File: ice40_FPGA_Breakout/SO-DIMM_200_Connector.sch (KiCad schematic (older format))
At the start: 21 parts

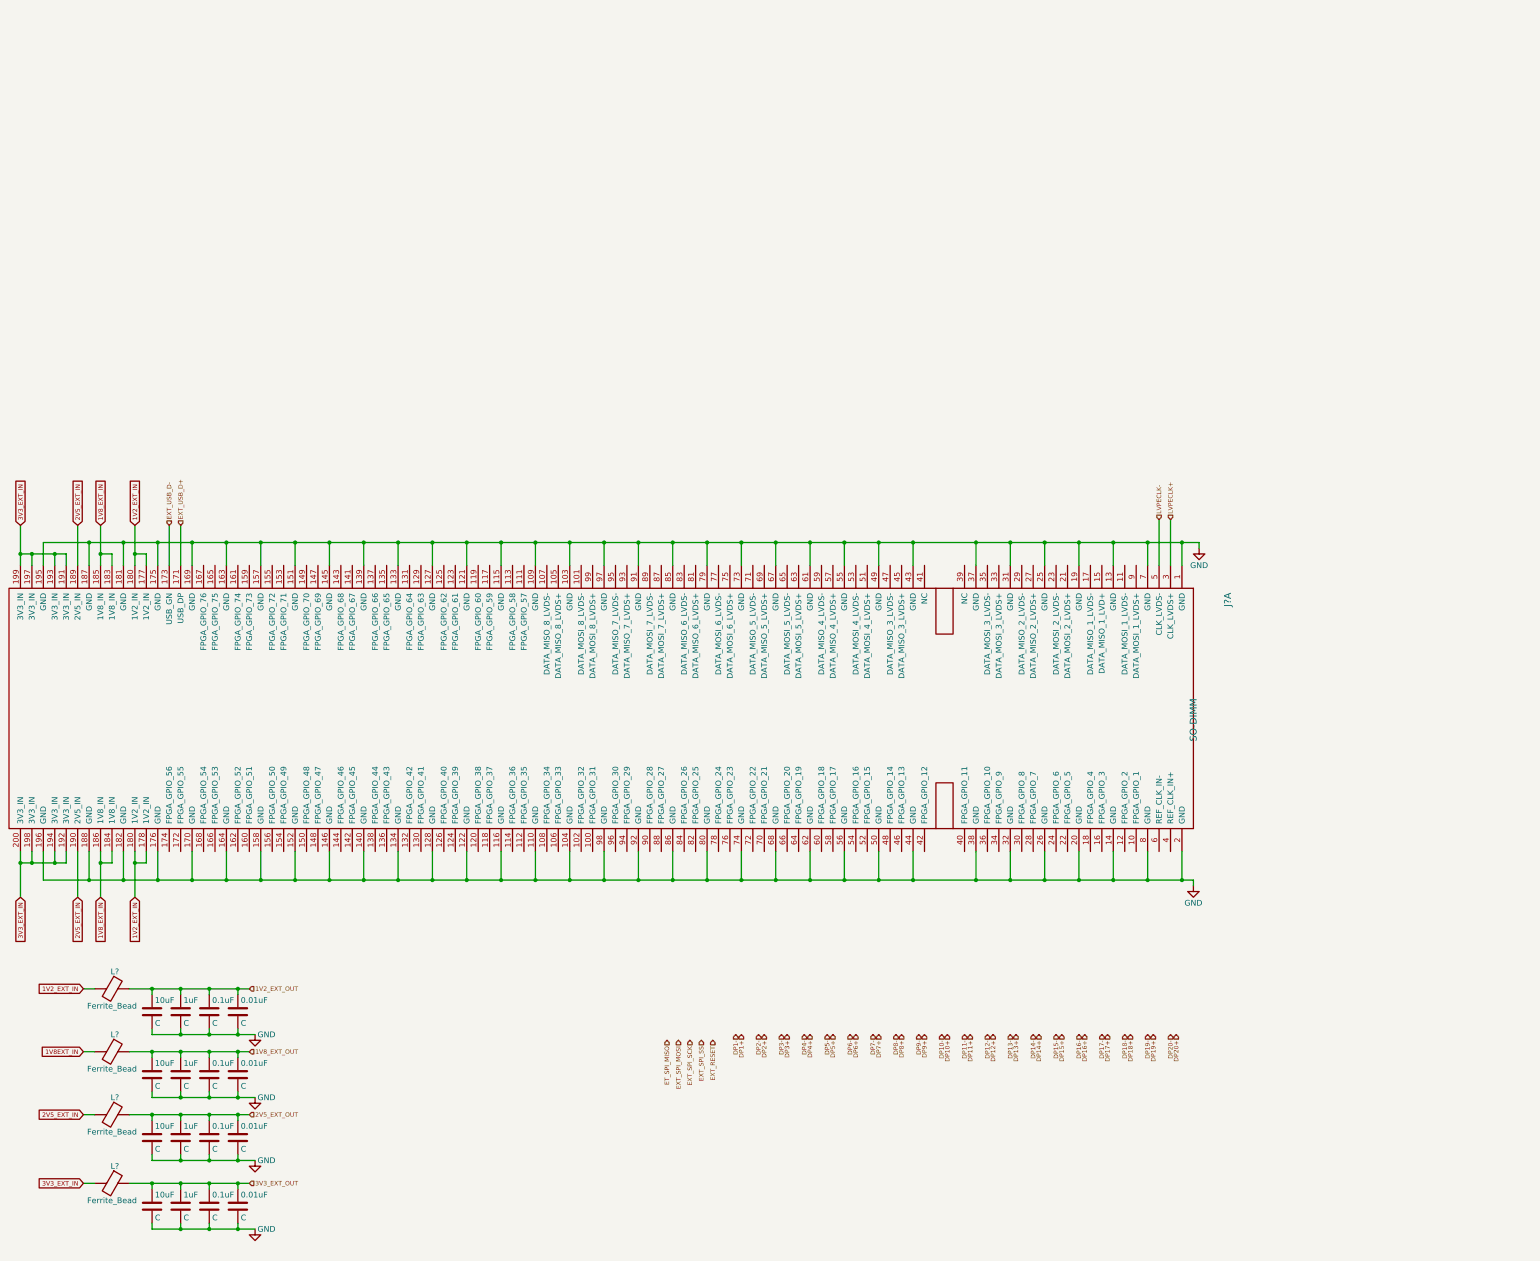
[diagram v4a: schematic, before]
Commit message: Component Annotated and R/C/Conn/TP CVPCB mapping
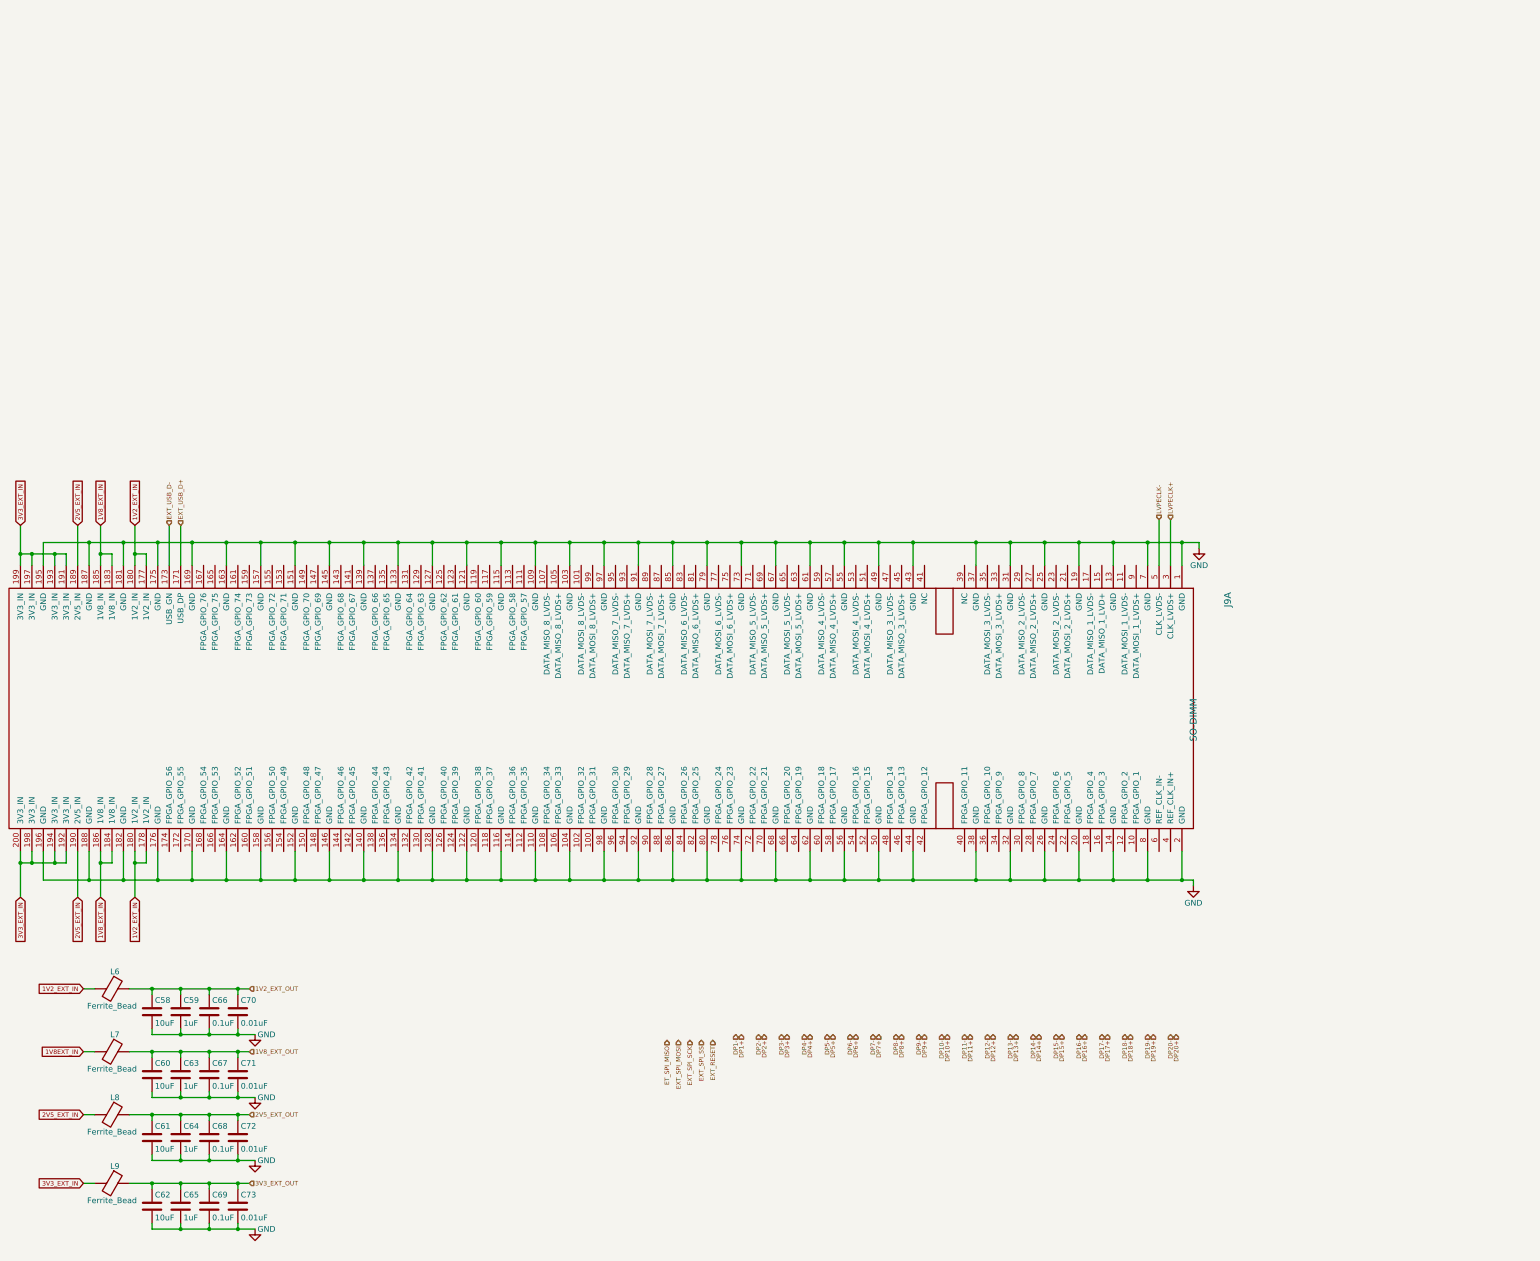
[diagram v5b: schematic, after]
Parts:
- C58, C60, C61, C62: renamed from 10uF; value C -> 10uF
- C59, C63, C64, C65: renamed from 1uF; value C -> 1uF
- C66, C67, C68, C69: renamed from 0.1uF; value C -> 0.1uF
- C70, C71, C72, C73: renamed from 0.01uF; value C -> 0.01uF
- gave numbers to parts that had none: 5
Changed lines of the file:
@@
 $EndDescr
 $Comp
-L SO-DIMM J?
+L SO-DIMM J9
 U 1 1 5A3A8985
 P 11200 2950
-F 0 "J?" H 10250 3100 60  0000 C CNN
+F 0 "J9" H 10250 3100 60  0000 C CNN
 F 1 "SO-DIMM" H 11300 2800 60  0000 C CNN
 F 2 "" H 11350 2950 60  0001 C CNN
@@
 $EndComp
 $Comp
-L C 10uF
+L C C58
 U 1 1 5A418459
 P 1950 5600
-F 0 "10uF" H 1975 5700 50  0000 L CNN
-F 1 "C" H 1975 5500 50  0000 L CNN
+F 0 "C58" H 1975 5700 50  0000 L CNN
+F 1 "10uF" H 1975 5500 50  0000 L CNN
 F 2 "" H 1988 5450 50  0001 C CNN
 F 3 "" H 1950 5600 50  0001 C CNN
@@
 $EndComp
 $Comp
-L C 1uF
+L C C59
 U 1 1 5A4184EA
 P 2200 5600
-F 0 "1uF" H 2225 5700 50  0000 L CNN
-F 1 "C" H 2225 5500 50  0000 L CNN
+F 0 "C59" H 2225 5700 50  0000 L CNN
+F 1 "1uF" H 2225 5500 50  0000 L CNN
 F 2 "" H 2238 5450 50  0001 C CNN
 F 3 "" H 2200 5600 50  0001 C CNN
@@
 $EndComp
 $Comp
-L C 0.1uF
+L C C66
 U 1 1 5A41850F
 P 2450 5600
-F 0 "0.1uF" H 2475 5700 50  0000 L CNN
-F 1 "C" H 2475 5500 50  0000 L CNN
+F 0 "C66" H 2475 5700 50  0000 L CNN
+F 1 "0.1uF" H 2475 5500 50  0000 L CNN
 F 2 "" H 2488 5450 50  0001 C CNN
 F 3 "" H 2450 5600 50  0001 C CNN
@@
 $EndComp
 $Comp
-L C 0.01uF
+L C C70
 U 1 1 5A418541
 P 2700 5600
-F 0 "0.01uF" H 2725 5700 50  0000 L CNN
-F 1 "C" H 2725 5500 50  0000 L CNN
+F 0 "C70" H 2725 5700 50  0000 L CNN
+F 1 "0.01uF" H 2725 5500 50  0000 L CNN
 F 2 "" H 2738 5450 50  0001 C CNN
 F 3 "" H 2700 5600 50  0001 C CNN
@@
 $EndComp
 $Comp
-L C 10uF
+L C C60
 U 1 1 5A41856A
 P 1950 6150
-F 0 "10uF" H 1975 6250 50  0000 L CNN
-F 1 "C" H 1975 6050 50  0000 L CNN
+F 0 "C60" H 1975 6250 50  0000 L CNN
+F 1 "10uF" H 1975 6050 50  0000 L CNN
 F 2 "" H 1988 6000 50  0001 C CNN
 F 3 "" H 1950 6150 50  0001 C CNN
@@
 $EndComp
 $Comp
-L C 1uF
+L C C63
 U 1 1 5A4185BC
 P 2200 6150
-F 0 "1uF" H 2225 6250 50  0000 L CNN
-F 1 "C" H 2225 6050 50  0000 L CNN
+F 0 "C63" H 2225 6250 50  0000 L CNN
+F 1 "1uF" H 2225 6050 50  0000 L CNN
 F 2 "" H 2238 6000 50  0001 C CNN
 F 3 "" H 2200 6150 50  0001 C CNN
@@
 $EndComp
 $Comp
-L C 0.1uF
+L C C67
 U 1 1 5A4185F9
 P 2450 6150
-F 0 "0.1uF" H 2475 6250 50  0000 L CNN
-F 1 "C" H 2475 6050 50  0000 L CNN
+F 0 "C67" H 2475 6250 50  0000 L CNN
+F 1 "0.1uF" H 2475 6050 50  0000 L CNN
 F 2 "" H 2488 6000 50  0001 C CNN
 F 3 "" H 2450 6150 50  0001 C CNN
@@
 $EndComp
 $Comp
-L C 0.01uF
+L C C71
 U 1 1 5A41862F
 P 2700 6150
-F 0 "0.01uF" H 2725 6250 50  0000 L CNN
-F 1 "C" H 2725 6050 50  0000 L CNN
+F 0 "C71" H 2725 6250 50  0000 L CNN
+F 1 "0.01uF" H 2725 6050 50  0000 L CNN
 F 2 "" H 2738 6000 50  0001 C CNN
 F 3 "" H 2700 6150 50  0001 C CNN
@@
 $EndComp
 $Comp
-L C 10uF
+L C C61
 U 1 1 5A418664
 P 1950 6700
-F 0 "10uF" H 1975 6800 50  0000 L CNN
-F 1 "C" H 1975 6600 50  0000 L CNN
+F 0 "C61" H 1975 6800 50  0000 L CNN
+F 1 "10uF" H 1975 6600 50  0000 L CNN
 F 2 "" H 1988 6550 50  0001 C CNN
 F 3 "" H 1950 6700 50  0001 C CNN
@@
 $EndComp
 $Comp
-L C 1uF
+L C C64
 U 1 1 5A4186B2
 P 2200 6700
-F 0 "1uF" H 2225 6800 50  0000 L CNN
-F 1 "C" H 2225 6600 50  0000 L CNN
+F 0 "C64" H 2225 6800 50  0000 L CNN
+F 1 "1uF" H 2225 6600 50  0000 L CNN
 F 2 "" H 2238 6550 50  0001 C CNN
 F 3 "" H 2200 6700 50  0001 C CNN
@@
 $EndComp
 $Comp
-L C 0.1uF
+L C C68
 U 1 1 5A4186E9
 P 2450 6700
-F 0 "0.1uF" H 2475 6800 50  0000 L CNN
-F 1 "C" H 2475 6600 50  0000 L CNN
+F 0 "C68" H 2475 6800 50  0000 L CNN
+F 1 "0.1uF" H 2475 6600 50  0000 L CNN
 F 2 "" H 2488 6550 50  0001 C CNN
 F 3 "" H 2450 6700 50  0001 C CNN
@@
 $EndComp
 $Comp
-L C 0.01uF
+L C C72
 U 1 1 5A418729
 P 2700 6700
-F 0 "0.01uF" H 2725 6800 50  0000 L CNN
-F 1 "C" H 2725 6600 50  0000 L CNN
+F 0 "C72" H 2725 6800 50  0000 L CNN
+F 1 "0.01uF" H 2725 6600 50  0000 L CNN
 F 2 "" H 2738 6550 50  0001 C CNN
 F 3 "" H 2700 6700 50  0001 C CNN
@@
 $EndComp
 $Comp
-L C 10uF
+L C C62
 U 1 1 5A418776
 P 1950 7300
-F 0 "10uF" H 1975 7400 50  0000 L CNN
-F 1 "C" H 1975 7200 50  0000 L CNN
+F 0 "C62" H 1975 7400 50  0000 L CNN
+F 1 "10uF" H 1975 7200 50  0000 L CNN
 F 2 "" H 1988 7150 50  0001 C CNN
 F 3 "" H 1950 7300 50  0001 C CNN
@@
 $EndComp
 $Comp
-L C 1uF
+L C C65
 U 1 1 5A418B7E
 P 2200 7300
-F 0 "1uF" H 2225 7400 50  0000 L CNN
-F 1 "C" H 2225 7200 50  0000 L CNN
+F 0 "C65" H 2225 7400 50  0000 L CNN
+F 1 "1uF" H 2225 7200 50  0000 L CNN
 F 2 "" H 2238 7150 50  0001 C CNN
 F 3 "" H 2200 7300 50  0001 C CNN
@@
 $EndComp
 $Comp
-L C 0.1uF
+L C C69
 U 1 1 5A418BC9
 P 2450 7300
-F 0 "0.1uF" H 2475 7400 50  0000 L CNN
-F 1 "C" H 2475 7200 50  0000 L CNN
+F 0 "C69" H 2475 7400 50  0000 L CNN
+F 1 "0.1uF" H 2475 7200 50  0000 L CNN
 F 2 "" H 2488 7150 50  0001 C CNN
 F 3 "" H 2450 7300 50  0001 C CNN
@@
 $EndComp
 $Comp
-L C 0.01uF
+L C C73
 U 1 1 5A418C13
 P 2700 7300
-F 0 "0.01uF" H 2725 7400 50  0000 L CNN
-F 1 "C" H 2725 7200 50  0000 L CNN
+F 0 "C73" H 2725 7400 50  0000 L CNN
+F 1 "0.01uF" H 2725 7200 50  0000 L CNN
 F 2 "" H 2738 7150 50  0001 C CNN
 F 3 "" H 2700 7300 50  0001 C CNN
@@
 2V5_EXT_IN
 $Comp
-L GND #PWR038
+L GND #PWR045
 U 1 1 5A41B6AD
 P 2850 5800
-F 0 "#PWR038" H 2850 5550 50  0001 C CNN
+F 0 "#PWR045" H 2850 5550 50  0001 C CNN
 F 1 "GND" H 2950 5800 50  0000 C CNN
 F 2 "" H 2850 5800 50  0001 C CNN
@@
 $EndComp
 $Comp
-L GND #PWR039
+L GND #PWR046
 U 1 1 5A41B7D9
 P 2850 6350
-F 0 "#PWR039" H 2850 6100 50  0001 C CNN
+F 0 "#PWR046" H 2850 6100 50  0001 C CNN
 F 1 "GND" H 2950 6350 50  0000 C CNN
 F 2 "" H 2850 6350 50  0001 C CNN
@@
 $EndComp
 $Comp
-L GND #PWR040
+L GND #PWR047
 U 1 1 5A41B927
 P 2850 7500
-F 0 "#PWR040" H 2850 7250 50  0001 C CNN
+F 0 "#PWR047" H 2850 7250 50  0001 C CNN
 F 1 "GND" H 2950 7500 50  0000 C CNN
 F 2 "" H 2850 7500 50  0001 C CNN
@@
 $EndComp
 $Comp
-L GND #PWR041
+L GND #PWR048
 U 1 1 5A41B976
 P 2850 6900
-F 0 "#PWR041" H 2850 6650 50  0001 C CNN
+F 0 "#PWR048" H 2850 6650 50  0001 C CNN
 F 1 "GND" H 2950 6900 50  0000 C CNN
 F 2 "" H 2850 6900 50  0001 C CNN
@@
 $EndComp
 $Comp
-L GND #PWR042
+L GND #PWR049
 U 1 1 5A41CA24
 P 11050 4500
-F 0 "#PWR042" H 11050 4250 50  0001 C CNN
+F 0 "#PWR049" H 11050 4250 50  0001 C CNN
 F 1 "GND" H 11050 4350 50  0000 C CNN
 F 2 "" H 11050 4500 50  0001 C CNN
@@
 Connection ~ 10950 1500
 $Comp
-L GND #PWR043
+L GND #PWR050
 U 1 1 5A421824
 P 11100 1550
-F 0 "#PWR043" H 11100 1300 50  0001 C CNN
+F 0 "#PWR050" H 11100 1300 50  0001 C CNN
 F 1 "GND" H 11100 1400 50  0000 C CNN
 F 2 "" H 11100 1550 50  0001 C CNN
@@
 	1300 4200 1300 4600
 $Comp
-L Ferrite_Bead L?
+L Ferrite_Bead L6
 U 1 1 5A42412E
 P 1600 5400
-F 0 "L?" V 1450 5425 50  0000 C CNN
+F 0 "L6" V 1450 5425 50  0000 C CNN
 F 1 "Ferrite_Bead" V 1750 5400 50  0000 C CNN
 F 2 "" V 1530 5400 50  0001 C CNN
@@
 $EndComp
 $Comp
-L Ferrite_Bead L?
+L Ferrite_Bead L7
 U 1 1 5A4241DD
 P 1600 5950
-F 0 "L?" V 1450 5975 50  0000 C CNN
+F 0 "L7" V 1450 5975 50  0000 C CNN
 F 1 "Ferrite_Bead" V 1750 5950 50  0000 C CNN
 F 2 "" V 1530 5950 50  0001 C CNN
@@
 $EndComp
 $Comp
-L Ferrite_Bead L?
+L Ferrite_Bead L8
 U 1 1 5A4242DA
 P 1600 6500
-F 0 "L?" V 1450 6525 50  0000 C CNN
+F 0 "L8" V 1450 6525 50  0000 C CNN
 F 1 "Ferrite_Bead" V 1750 6500 50  0000 C CNN
 F 2 "" V 1530 6500 50  0001 C CNN
@@
 $EndComp
 $Comp
-L Ferrite_Bead L?
+L Ferrite_Bead L9
 U 1 1 5A424340
 P 1600 7100
-F 0 "L?" V 1450 7125 50  0000 C CNN
+F 0 "L9" V 1450 7125 50  0000 C CNN
 F 1 "Ferrite_Bead" V 1750 7100 50  0000 C CNN
 F 2 "" V 1530 7100 50  0001 C CNN

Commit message: schematic clean up, label aligned
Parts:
- C58, C59, C60, C61, C62, C63, C64, C65: footprint (none) -> Capacitor_SMD:C_0603_1608Metric
- C66, C67, C68, C69, C70, C71, C72, C73: footprint (none) -> Capacitor_SMD:C_0402_1005Metric
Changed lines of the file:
@@
 F 0 "C58" H 1975 5700 50  0000 L CNN
 F 1 "10uF" H 1975 5500 50  0000 L CNN
-F 2 "" H 1988 5450 50  0001 C CNN
+F 2 "Capacitor_SMD:C_0603_1608Metric" H 1988 5450 50  0001 C CNN
 F 3 "" H 1950 5600 50  0001 C CNN
 	1    1950 5600
@@
 F 0 "C59" H 2225 5700 50  0000 L CNN
 F 1 "1uF" H 2225 5500 50  0000 L CNN
-F 2 "" H 2238 5450 50  0001 C CNN
+F 2 "Capacitor_SMD:C_0603_1608Metric" H 2238 5450 50  0001 C CNN
 F 3 "" H 2200 5600 50  0001 C CNN
 	1    2200 5600
@@
 F 0 "C66" H 2475 5700 50  0000 L CNN
 F 1 "0.1uF" H 2475 5500 50  0000 L CNN
-F 2 "" H 2488 5450 50  0001 C CNN
+F 2 "Capacitor_SMD:C_0402_1005Metric" H 2488 5450 50  0001 C CNN
 F 3 "" H 2450 5600 50  0001 C CNN
 	1    2450 5600
@@
 F 0 "C70" H 2725 5700 50  0000 L CNN
 F 1 "0.01uF" H 2725 5500 50  0000 L CNN
-F 2 "" H 2738 5450 50  0001 C CNN
+F 2 "Capacitor_SMD:C_0402_1005Metric" H 2738 5450 50  0001 C CNN
 F 3 "" H 2700 5600 50  0001 C CNN
 	1    2700 5600
@@
 F 0 "C60" H 1975 6250 50  0000 L CNN
 F 1 "10uF" H 1975 6050 50  0000 L CNN
-F 2 "" H 1988 6000 50  0001 C CNN
+F 2 "Capacitor_SMD:C_0603_1608Metric" H 1988 6000 50  0001 C CNN
 F 3 "" H 1950 6150 50  0001 C CNN
 	1    1950 6150
@@
 F 0 "C63" H 2225 6250 50  0000 L CNN
 F 1 "1uF" H 2225 6050 50  0000 L CNN
-F 2 "" H 2238 6000 50  0001 C CNN
+F 2 "Capacitor_SMD:C_0603_1608Metric" H 2238 6000 50  0001 C CNN
 F 3 "" H 2200 6150 50  0001 C CNN
 	1    2200 6150
@@
 F 0 "C67" H 2475 6250 50  0000 L CNN
 F 1 "0.1uF" H 2475 6050 50  0000 L CNN
-F 2 "" H 2488 6000 50  0001 C CNN
+F 2 "Capacitor_SMD:C_0402_1005Metric" H 2488 6000 50  0001 C CNN
 F 3 "" H 2450 6150 50  0001 C CNN
 	1    2450 6150
@@
 F 0 "C71" H 2725 6250 50  0000 L CNN
 F 1 "0.01uF" H 2725 6050 50  0000 L CNN
-F 2 "" H 2738 6000 50  0001 C CNN
+F 2 "Capacitor_SMD:C_0402_1005Metric" H 2738 6000 50  0001 C CNN
 F 3 "" H 2700 6150 50  0001 C CNN
 	1    2700 6150
@@
 F 0 "C61" H 1975 6800 50  0000 L CNN
 F 1 "10uF" H 1975 6600 50  0000 L CNN
-F 2 "" H 1988 6550 50  0001 C CNN
+F 2 "Capacitor_SMD:C_0603_1608Metric" H 1988 6550 50  0001 C CNN
 F 3 "" H 1950 6700 50  0001 C CNN
 	1    1950 6700
@@
 F 0 "C64" H 2225 6800 50  0000 L CNN
 F 1 "1uF" H 2225 6600 50  0000 L CNN
-F 2 "" H 2238 6550 50  0001 C CNN
+F 2 "Capacitor_SMD:C_0603_1608Metric" H 2238 6550 50  0001 C CNN
 F 3 "" H 2200 6700 50  0001 C CNN
 	1    2200 6700
@@
 F 0 "C68" H 2475 6800 50  0000 L CNN
 F 1 "0.1uF" H 2475 6600 50  0000 L CNN
-F 2 "" H 2488 6550 50  0001 C CNN
+F 2 "Capacitor_SMD:C_0402_1005Metric" H 2488 6550 50  0001 C CNN
 F 3 "" H 2450 6700 50  0001 C CNN
 	1    2450 6700
@@
 F 0 "C72" H 2725 6800 50  0000 L CNN
 F 1 "0.01uF" H 2725 6600 50  0000 L CNN
-F 2 "" H 2738 6550 50  0001 C CNN
+F 2 "Capacitor_SMD:C_0402_1005Metric" H 2738 6550 50  0001 C CNN
 F 3 "" H 2700 6700 50  0001 C CNN
 	1    2700 6700
@@
 F 0 "C62" H 1975 7400 50  0000 L CNN
 F 1 "10uF" H 1975 7200 50  0000 L CNN
-F 2 "" H 1988 7150 50  0001 C CNN
+F 2 "Capacitor_SMD:C_0603_1608Metric" H 1988 7150 50  0001 C CNN
 F 3 "" H 1950 7300 50  0001 C CNN
 	1    1950 7300
@@
 F 0 "C65" H 2225 7400 50  0000 L CNN
 F 1 "1uF" H 2225 7200 50  0000 L CNN
-F 2 "" H 2238 7150 50  0001 C CNN
+F 2 "Capacitor_SMD:C_0603_1608Metric" H 2238 7150 50  0001 C CNN
 F 3 "" H 2200 7300 50  0001 C CNN
 	1    2200 7300
@@
 F 0 "C69" H 2475 7400 50  0000 L CNN
 F 1 "0.1uF" H 2475 7200 50  0000 L CNN
-F 2 "" H 2488 7150 50  0001 C CNN
+F 2 "Capacitor_SMD:C_0402_1005Metric" H 2488 7150 50  0001 C CNN
 F 3 "" H 2450 7300 50  0001 C CNN
 	1    2450 7300
@@
 F 0 "C73" H 2725 7400 50  0000 L CNN
 F 1 "0.01uF" H 2725 7200 50  0000 L CNN
-F 2 "" H 2738 7150 50  0001 C CNN
+F 2 "Capacitor_SMD:C_0402_1005Metric" H 2738 7150 50  0001 C CNN
 F 3 "" H 2700 7300 50  0001 C CNN
 	1    2700 7300

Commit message: assigned footprint to each component
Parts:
- J9: footprint (none) -> GTI_Footprint_Lib:SO_DIMM_200
- L6, L7, L8, L9: footprint (none) -> Inductor_SMD:L_0603_1608Metric
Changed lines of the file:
@@
 F 0 "J9" H 10250 3100 60  0000 C CNN
 F 1 "SO-DIMM" H 11300 2800 60  0000 C CNN
-F 2 "" H 11350 2950 60  0001 C CNN
+F 2 "GTI_Footprint_Lib:SO_DIMM_200" H 11350 2950 60  0001 C CNN
 F 3 "" H 11350 2950 60  0001 C CNN
 	1    11200 2950
@@
 F 0 "L6" V 1450 5425 50  0000 C CNN
 F 1 "Ferrite_Bead" V 1750 5400 50  0000 C CNN
-F 2 "" V 1530 5400 50  0001 C CNN
+F 2 "Inductor_SMD:L_0603_1608Metric" V 1530 5400 50  0001 C CNN
 F 3 "" H 1600 5400 50  0001 C CNN
 	1    1600 5400
@@
 F 0 "L7" V 1450 5975 50  0000 C CNN
 F 1 "Ferrite_Bead" V 1750 5950 50  0000 C CNN
-F 2 "" V 1530 5950 50  0001 C CNN
+F 2 "Inductor_SMD:L_0603_1608Metric" V 1530 5950 50  0001 C CNN
 F 3 "" H 1600 5950 50  0001 C CNN
 	1    1600 5950
@@
 F 0 "L8" V 1450 6525 50  0000 C CNN
 F 1 "Ferrite_Bead" V 1750 6500 50  0000 C CNN
-F 2 "" V 1530 6500 50  0001 C CNN
+F 2 "Inductor_SMD:L_0603_1608Metric" V 1530 6500 50  0001 C CNN
 F 3 "" H 1600 6500 50  0001 C CNN
 	1    1600 6500
@@
 F 0 "L9" V 1450 7125 50  0000 C CNN
 F 1 "Ferrite_Bead" V 1750 7100 50  0000 C CNN
-F 2 "" V 1530 7100 50  0001 C CNN
+F 2 "Inductor_SMD:L_0603_1608Metric" V 1530 7100 50  0001 C CNN
 F 3 "" H 1600 7100 50  0001 C CNN
 	1    1600 7100
